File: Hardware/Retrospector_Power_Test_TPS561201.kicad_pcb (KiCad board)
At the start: 2 copper layers, 27 x 21 mm, 22 parts, among them J2 Eurorack_10_pin_power, U1 TPS561201, U2 LD1117-3.3-4Tab

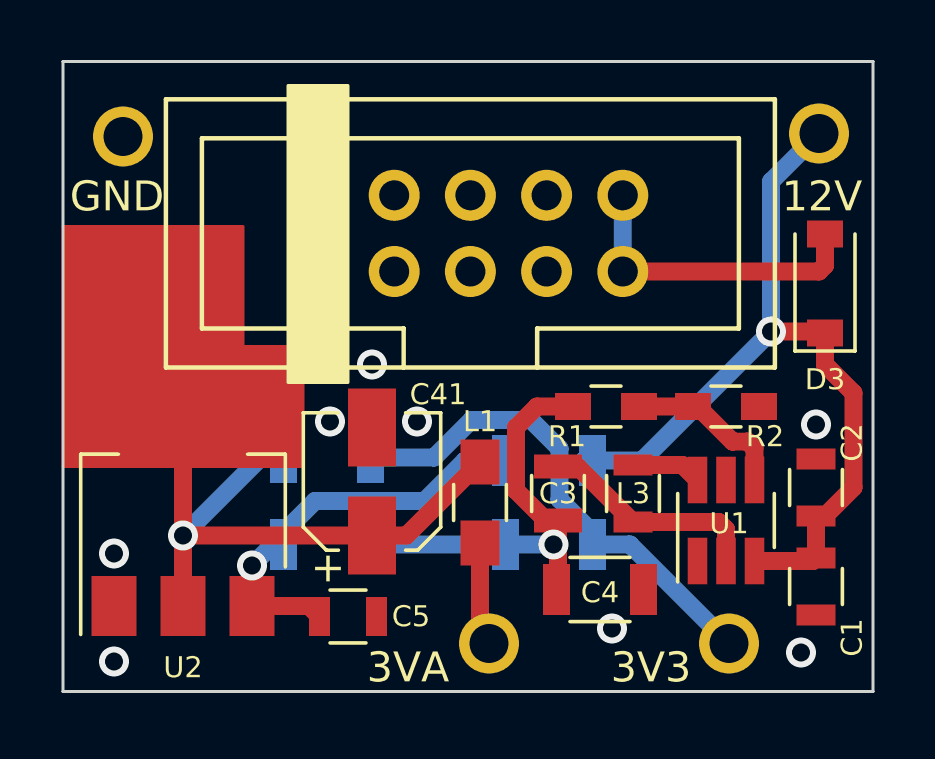
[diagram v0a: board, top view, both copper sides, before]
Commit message: Debugging DAC clock issues when using FMC to control SDRAM
Workaround is to switch the clock for the I2S DAC to peripheral clock (also used by ADC at present)
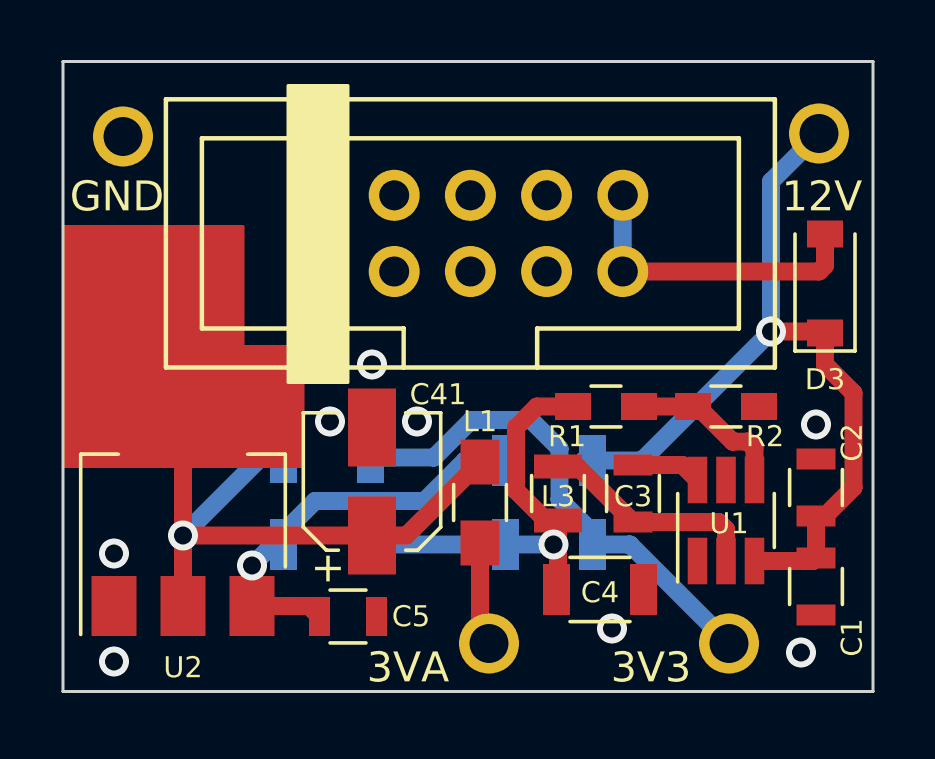
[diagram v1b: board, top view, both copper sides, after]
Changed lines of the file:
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@@
     (47 F.CrtYd user hide)
     (48 B.Fab user hide)
-    (49 F.Fab user hide)
+    (49 F.Fab user)
   )
   (setup
@@
     (tags "resistor 0805")
     (attr smd)
-    (fp_text reference L3 (at 0 -2.5 180) (layer F.SilkS)
+    (fp_text reference L3 (at 0.1 0 180) (layer F.SilkS)
       (effects (font (size 0.7 0.7) (thickness 0.1)))
     )
@@
     (tags "resistor 0805")
     (attr smd)
-    (fp_text reference C3 (at 0 -2.5 180) (layer F.SilkS)
-      (effects (font (size 0.7 0.7) (thickness 0.1)))
-    )
+    (fp_text reference C3 (at -0.1 0 180) (layer F.SilkS)
+      (effects (font (size 0.7 0.7) (thickness 0.1)))
+    )
